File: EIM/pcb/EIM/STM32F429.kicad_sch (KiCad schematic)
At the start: 33 parts, among them J1 SWD, J2 FTSH-107-01-F-DV-K, SW1 RESET, U1 STM32F429ZITx, X1 ASE-8.000MHz, X2 ECS-327-32.768kHz

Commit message: added Arjun's comments, assigned some MCU pins
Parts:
- removed C13: 10u/X5R, Capacitor_SMD:C_1206_3216Metric_Pad1.33x1.80mm_HandSolder, symbol Device:C
- added C19: 10u/X7R/50V, Capacitor_SMD:C_1206_3216Metric_Pad1.33x1.80mm_HandSolder, symbol Device:C
- added C54: 100n, Capacitor_SMD:C_0805_2012Metric_Pad1.18x1.45mm_HandSolder, symbol Device:C
- added SW2: BOOT, Button_Switch_SMD:SW_SPST_PTS645, symbol Switch:SW_Push
- renumbered C19 to C1, C5 to C10, C6 to C11, C7 to C12, C8 to C13, C9 to C14, C10 to C15, C11 to C16, C12 to C17, C21 to C18, C18 to C2, C15 to C20, C16 to C21, C17 to C3, C14 to C4, C1 to C5, C2 to C6, C20 to C7, C3 to C8, C4 to C9, J2 to J5, J1 to J6, R4 to R10, R5 to R11, R1 to R7, R2 to R8, R3 to R9
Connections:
- net +3V3: now also C19.1, C54.1, SW2.1
- net GND: now also C19.2
- net USART2_RX: now also U1.122 (PD6); no longer U1.37 (PA3)
- net USART2_TX: now also U1.119 (PD5); no longer U1.36 (PA2)
- net USART4_TX: now reaches U1.111 (PC10)
- net USART4_RX: now reaches U1.112 (PC11)
- net SPI2_SCK: now reaches U1.117 (PD3)
- net PD4: now reaches U1.118 (PD4)
- net I2C1_SCL: now reaches U1.136 (PB6)
- net I2C1_SDA: now reaches U1.137 (PB7)
- net at R7.2, U1.138 (BOOT0): now also C54.2, SW2.2
- net ADC1_IN10: now reaches U1.26 (PC0)
- net ADC1_IN11: now reaches U1.27 (PC1)
- net ADC1_IN12: now reaches U1.28 (PC2)
- net ADC1_IN13: now reaches U1.29 (PC3)
- net ADC1_IN0: now reaches U1.34 (PA0)
- net ADC1_IN1: now reaches U1.35 (PA1)
- net ADC1_IN5: now reaches U1.41 (PA5)
- net ADC1_IN6: now reaches U1.42 (PA6)
- net ADC1_IN7: now reaches U1.43 (PA7)
- net ADC1_IN8: now reaches U1.46 (PB0)
- net ADC1_IN9: now reaches U1.47 (PB1)
- net PB2/BOOT1: now reaches U1.48 (PB2)
- net SPI2_MISO: now reaches U1.75 (PB14)
- net SPI2_MOSI: now reaches U1.76 (PB15)
- net PA4 renamed ADC1_IN4
- new net ADC1_IN2: U1.36 (PA2)
- new net ADC1_IN3: U1.37 (PA3)
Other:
- moved on the sheet: R7

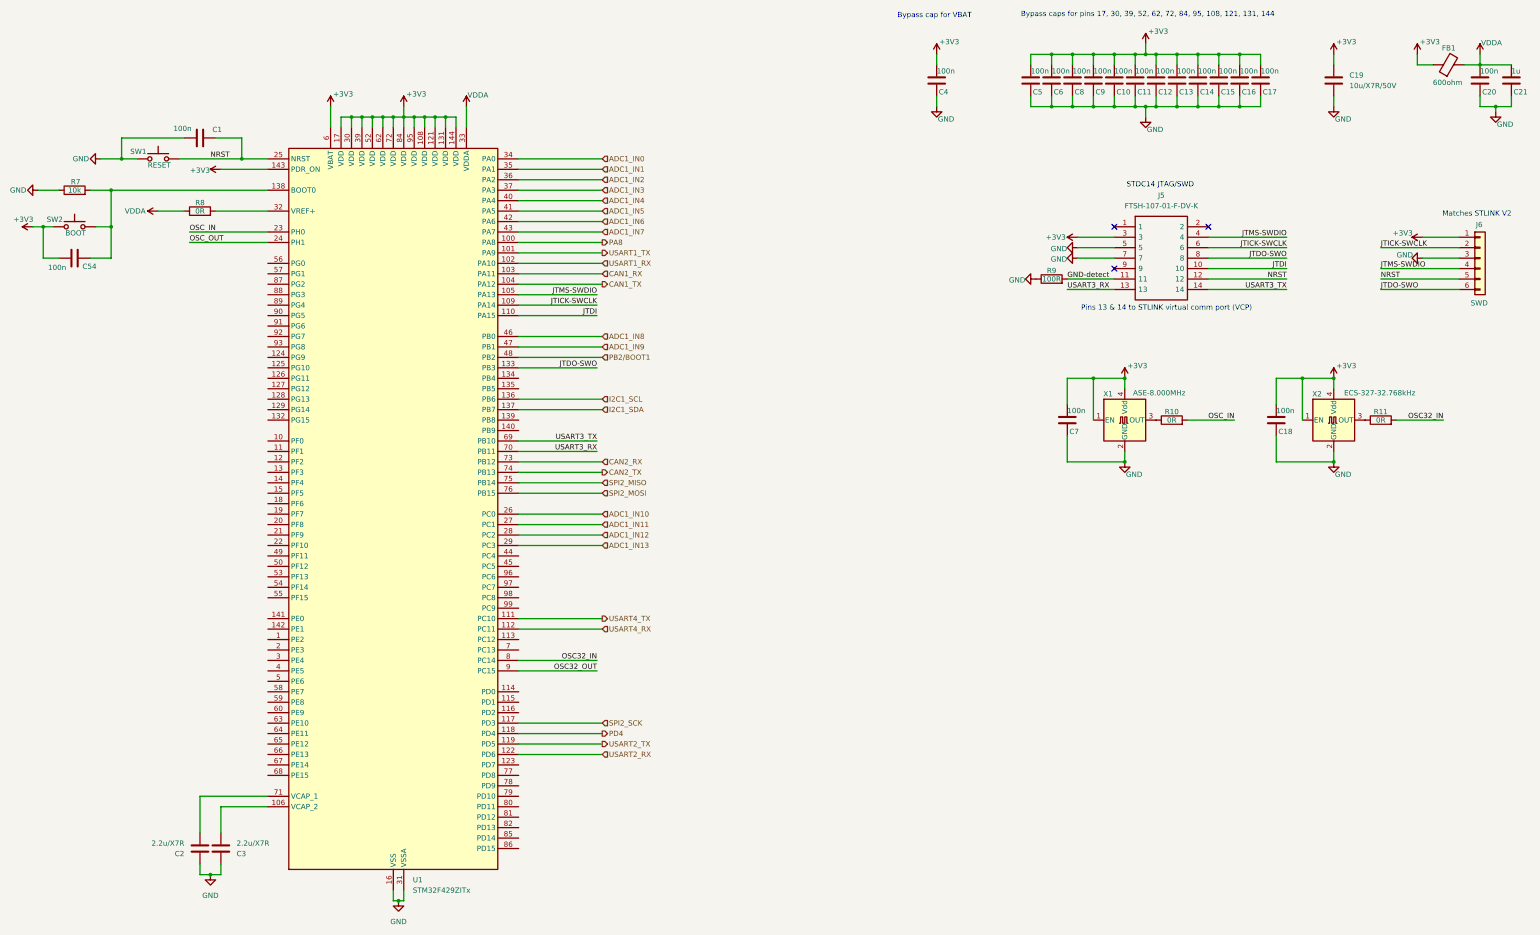
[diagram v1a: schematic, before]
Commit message: Layout 75% done, before 8V bus deletion
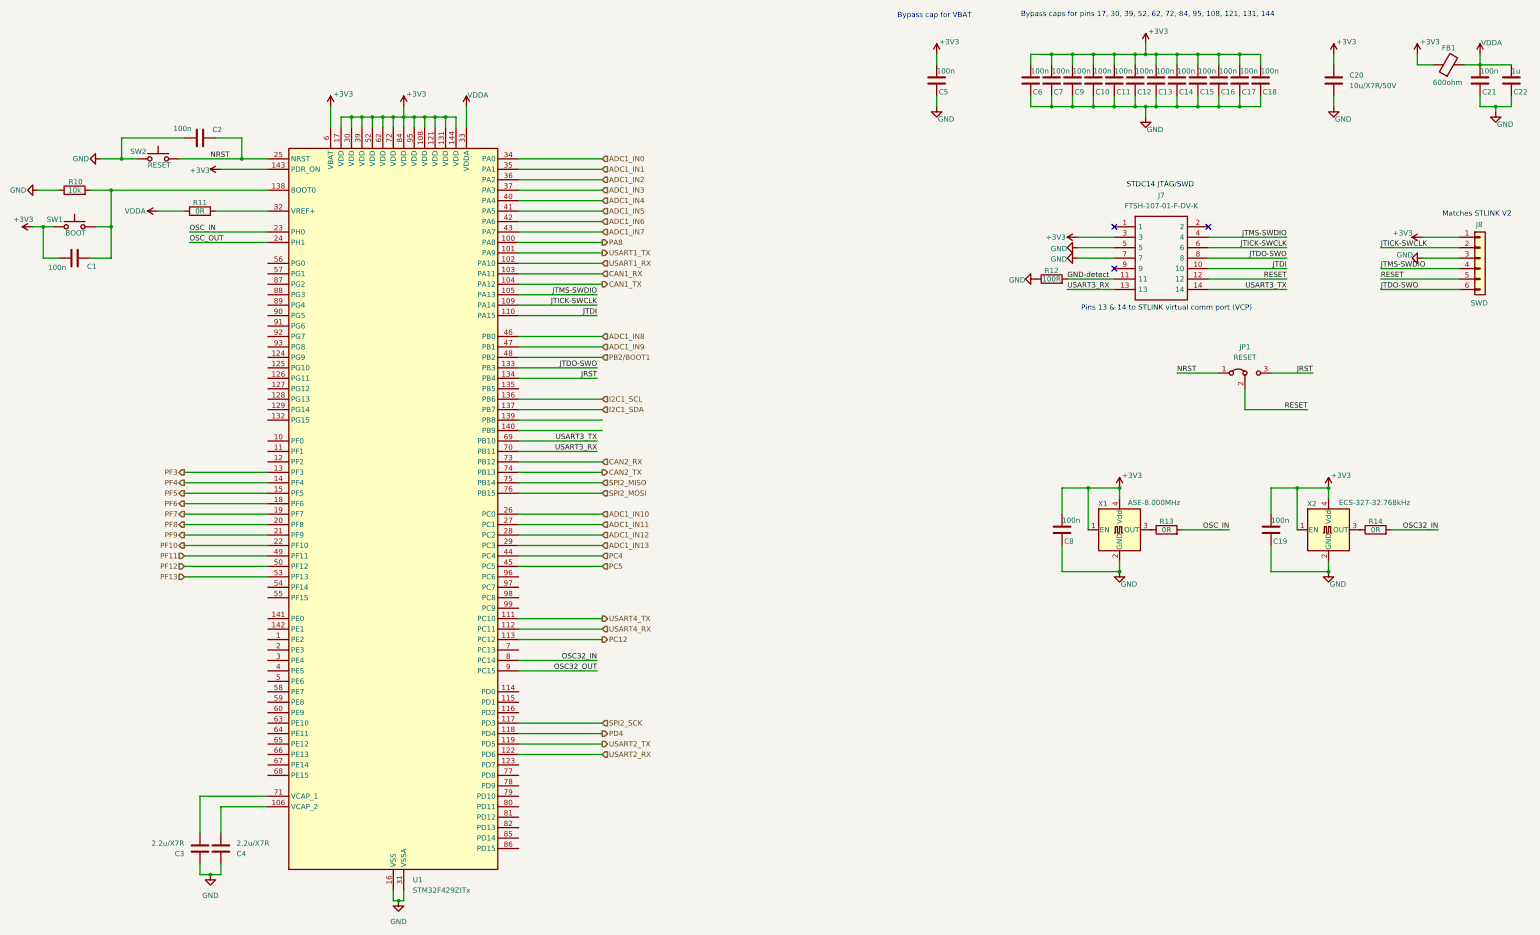
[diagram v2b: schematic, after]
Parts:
- added JP1: RESET, Jumper:SolderJumper-3_P1.3mm_Bridged12_RoundedPad1.0x1.5mm, symbol Jumper:Jumper_3_Bridged12
- renumbered C54 to C1, C9 to C10, C10 to C11, C11 to C12, C12 to C13, C13 to C14, C14 to C15, C15 to C16, C16 to C17, C17 to C18, C18 to C19, C1 to C2, C19 to C20, C20 to C21, C21 to C22, C2 to C3, C3 to C4, C4 to C5, C5 to C6, C6 to C7, C7 to C8, C8 to C9, J5 to J7, J6 to J8, R7 to R10, R8 to R11, R9 to R12, R10 to R13, R11 to R14, SW2 to SW1, SW1 to SW2
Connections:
- net NRST: now also JP1.1 (A); no longer J7.12, J8.5 (Pin_5)
- net PC12: now reaches U1.113 (PC12)
- net PF3: now reaches U1.13 (PF3)
- net JRST: now reaches U1.134 (PB4)
- net JRST: now also JP1.3 (B)
- net PF4: now reaches U1.14 (PF4)
- net PF5: now reaches U1.15 (PF5)
- net PF6: now reaches U1.18 (PF6)
- net PF7: now reaches U1.19 (PF7)
- net PF8: now reaches U1.20 (PF8)
- net PF9: now reaches U1.21 (PF9)
- net PF10: now reaches U1.22 (PF10)
- net PC4: now reaches U1.44 (PC4)
- net PC5: now reaches U1.45 (PC5)
- net PF11: now reaches U1.49 (PF11)
- net PF12: now reaches U1.50 (PF12)
- net PF13: now reaches U1.53 (PF13)
- new net RESET: J7.12, J8.5 (Pin_5), JP1.2 (C)
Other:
- moved on the sheet: C19, C8, R13, R14, X1, X2

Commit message: All components placed and pins assigned.
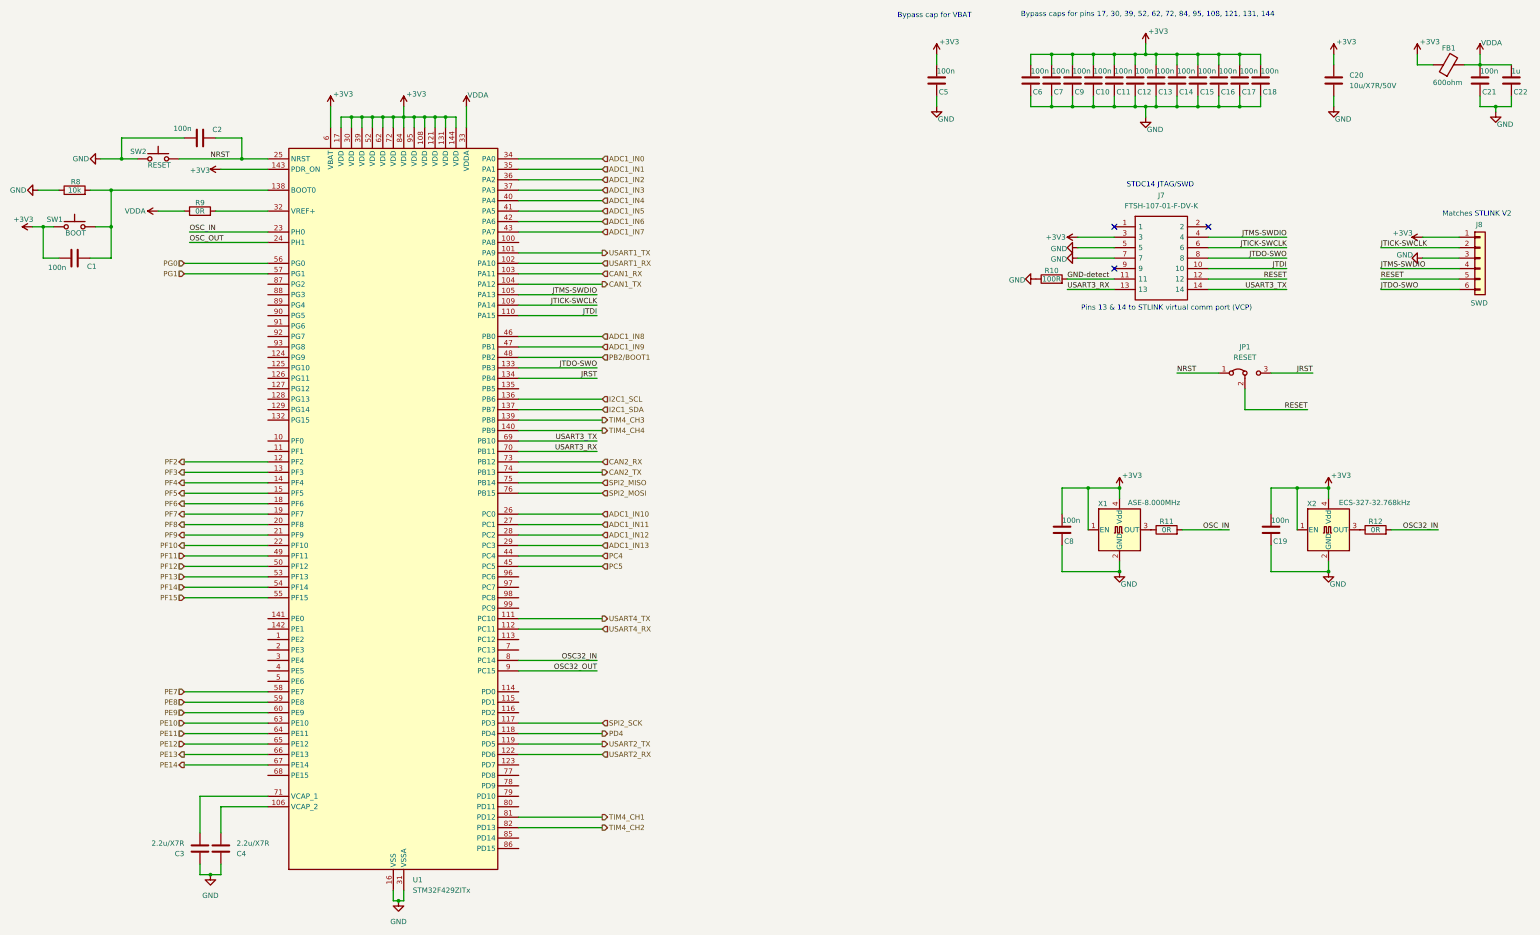
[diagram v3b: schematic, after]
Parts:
- renumbered R12 to R10, R13 to R11, R14 to R12, R10 to R8, R11 to R9
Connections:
- net PF2: now reaches U1.12 (PF2)
- net TIM4_CH3: now reaches U1.139 (PB8)
- net TIM4_CH4: now reaches U1.140 (PB9)
- net PF14: now reaches U1.54 (PF14)
- net PF15: now reaches U1.55 (PF15)
- net PG0: now reaches U1.56 (PG0)
- net PG1: now reaches U1.57 (PG1)
- net PE7: now reaches U1.58 (PE7)
- net PE8: now reaches U1.59 (PE8)
- net PE9: now reaches U1.60 (PE9)
- net PE10: now reaches U1.63 (PE10)
- net PE11: now reaches U1.64 (PE11)
- net PE12: now reaches U1.65 (PE12)
- net PE13: now reaches U1.66 (PE13)
- net PE14: now reaches U1.67 (PE14)
- net TIM4_CH1: now reaches U1.81 (PD12)
- net TIM4_CH2: now reaches U1.82 (PD13)
- net PA8: no longer names the net of U1.100 (PA8)
- net PC12: no longer names the net of U1.113 (PC12)

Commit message: Board data as ordered on 1-15-25
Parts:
- R10: value 100R -> 120R
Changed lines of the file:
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@@
 			)
 		)
-		(property "Value" "100R"
+		(property "Value" "120R"
 			(at 269.24 91.44 90)
 			(effects
